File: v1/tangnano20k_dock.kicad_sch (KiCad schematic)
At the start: 54 parts, among them J1 Mini-DIN-6, J2 Conn_01x02, J3 DB15_Female_HighDensity_Mount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, J4 DB9_Male_MountingHoles, J5 Conn_02x10_Odd_Even, J6 Conn_02x10_Odd_Even, J7 RCA, J8 FCR684205T, J9 AudioJack3, U1 TXS0104E, U2 TangNano20K, U3 CS4354

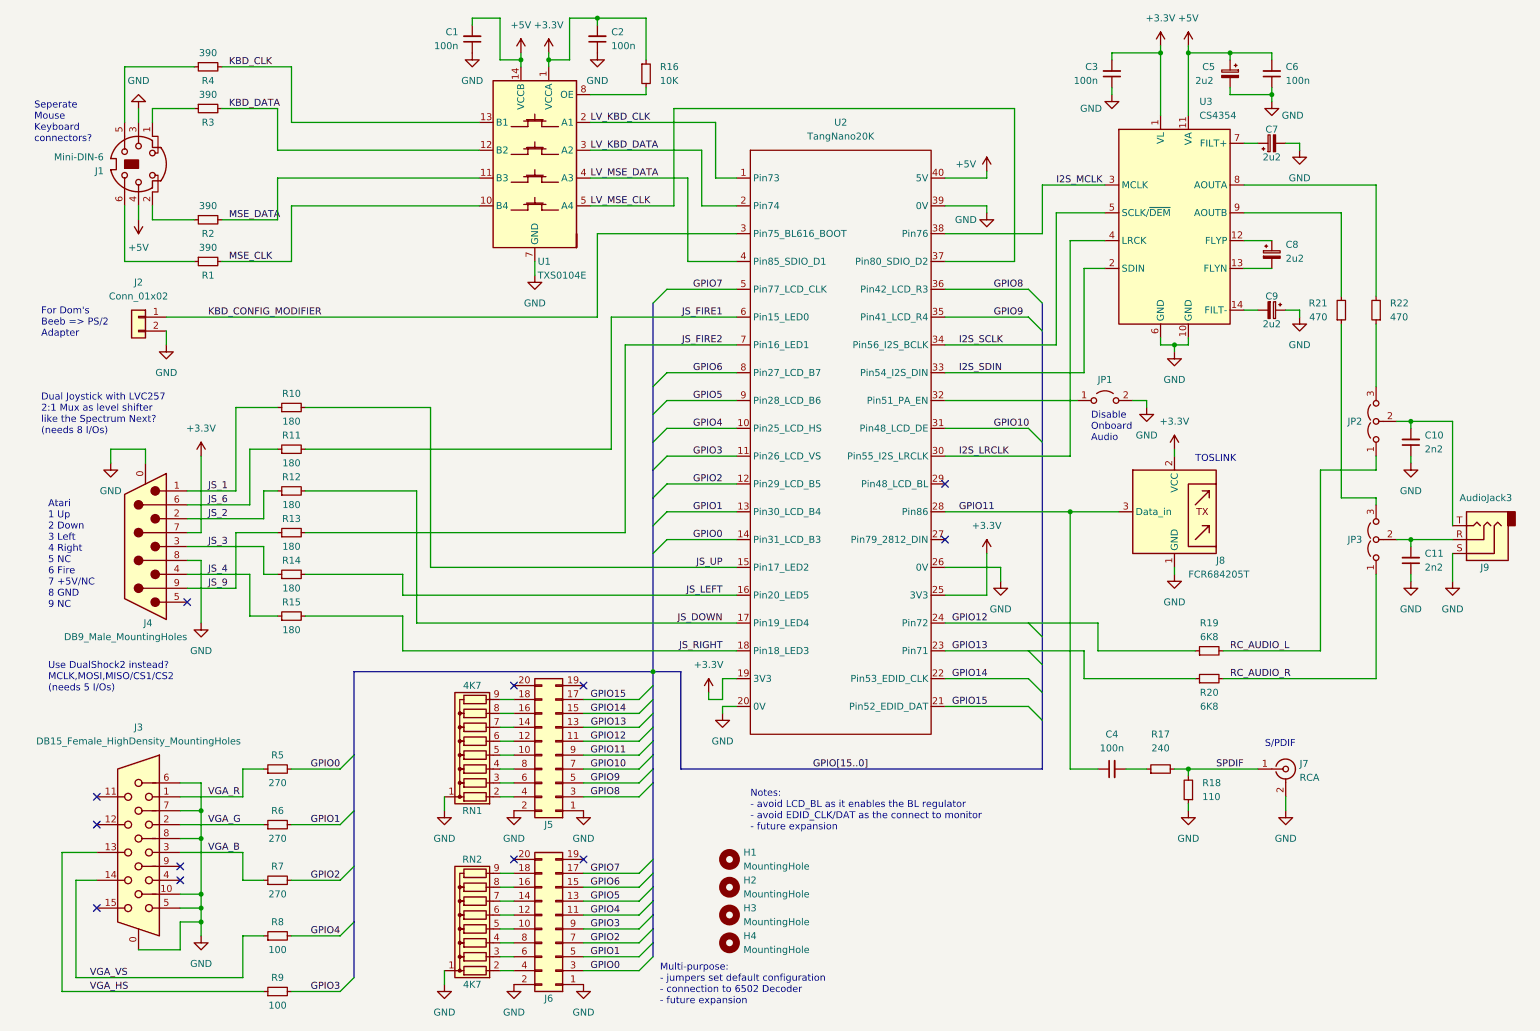
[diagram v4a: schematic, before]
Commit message: Start again, using 1206 SMT
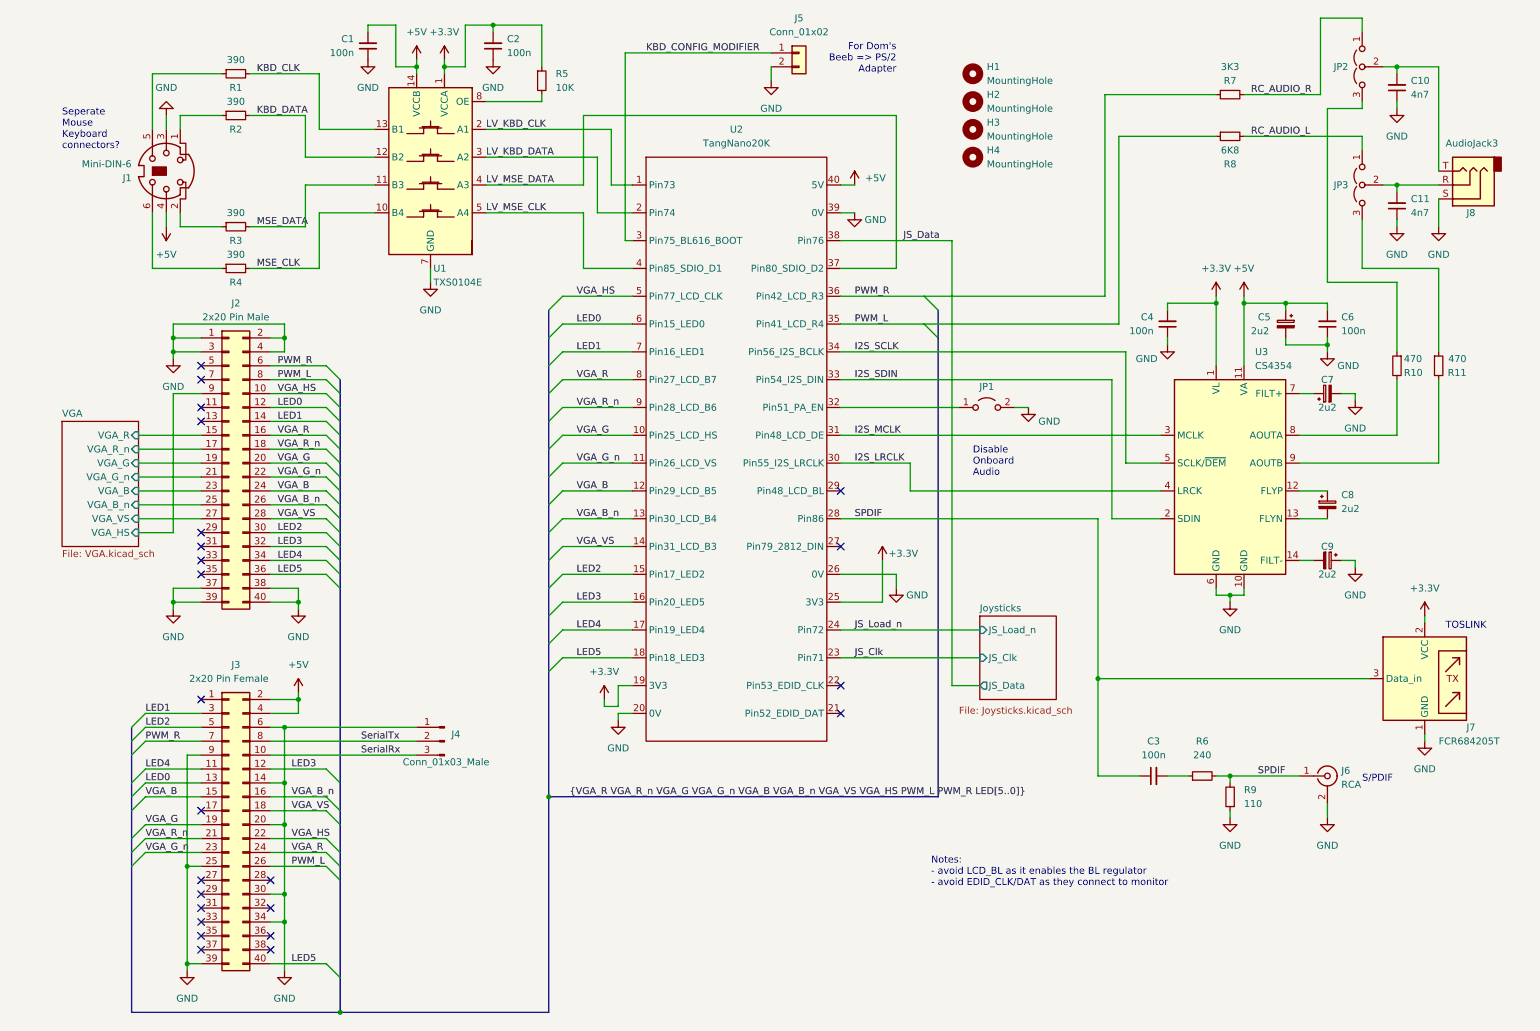
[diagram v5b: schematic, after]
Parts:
- removed J3: DB15_Female_HighDensity_MountingHoles, TangNano20k:DSUB-15-HD_Female_Horizontal_P2.29x1.98mm_EdgePinOffset8.35mm_Housed_MountingHolesOffset10.89mm, symbol Connector:DB15_Female_HighDensity_MountingHoles
- removed J4: DB9_Male_MountingHoles, Connector_Dsub:DSUB-9_Male_Horizontal_P2.77x2.84mm_EdgePinOffset7.70mm_Housed_MountingHolesOffset9.12mm, symbol Connector:DB9_Male_MountingHoles
- removed J5, J6: Conn_02x10_Odd_Even, Connector_PinHeader_2.54mm:PinHeader_2x10_P2.54mm_Vertical, symbol Connector_Generic:Conn_02x10_Odd_Even
- removed R10, R11, R12, R13, R14, R15: 180, Resistor_THT:R_Axial_DIN0207_L6.3mm_D2.5mm_P10.16mm_Horizontal, symbol Device:R_Small
- removed R5, R6, R7: 270, Resistor_THT:R_Axial_DIN0207_L6.3mm_D2.5mm_P10.16mm_Horizontal, symbol Device:R_Small
- removed R8, R9: 100, Resistor_THT:R_Axial_DIN0207_L6.3mm_D2.5mm_P10.16mm_Horizontal, symbol Device:R_Small
- removed RN1, RN2: 4K7, Resistor_THT:R_Array_SIP9, symbol Device:R_Network08
- added J2: 2x20 Pin Male, Connector_PinHeader_2.54mm:PinHeader_2x20_P2.54mm_Vertical, symbol Connector_Generic:Conn_02x20_Odd_Even
- added J3: 2x20 Pin Female, Connector_PinSocket_2.54mm:PinSocket_2x20_P2.54mm_Vertical, symbol Connector_Generic:Conn_02x20_Odd_Even
- added J4: Conn_01x03_Male, Connector_PinHeader_2.54mm:PinHeader_1x03_P2.54mm_Vertical, symbol Connector:Conn_01x03_Male
- C1, C2, C6: footprint Capacitor_THT:C_Disc_D4.3mm_W1.9mm_P5.00mm -> Capacitor_SMD:C_1206_3216Metric_Pad1.33x1.80mm_HandSolder
- C10, C11: value 2n2 -> 4n7; footprint Capacitor_THT:C_Disc_D5.0mm_W2.5mm_P2.50mm -> Capacitor_SMD:C_1206_3216Metric_Pad1.33x1.80mm_HandSolder
- C3: renamed from C4; footprint Capacitor_THT:C_Disc_D4.3mm_W1.9mm_P5.00mm -> Capacitor_SMD:C_1206_3216Metric_Pad1.33x1.80mm_HandSolder
- C4: renamed from C3; footprint Capacitor_THT:C_Disc_D4.3mm_W1.9mm_P5.00mm -> Capacitor_SMD:C_1206_3216Metric_Pad1.33x1.80mm_HandSolder
- C5, C7, C8, C9: footprint Capacitor_THT:CP_Radial_D5.0mm_P2.50mm -> Capacitor_SMD:C_1206_3216Metric_Pad1.33x1.80mm_HandSolder
- R1: renamed from R4; footprint Resistor_THT:R_Axial_DIN0207_L6.3mm_D2.5mm_P10.16mm_Horizontal -> Resistor_SMD:R_1206_3216Metric_Pad1.30x1.75mm_HandSolder
- R10: renamed from R22; footprint Resistor_THT:R_Axial_DIN0207_L6.3mm_D2.5mm_P10.16mm_Horizontal -> Resistor_SMD:R_1206_3216Metric_Pad1.30x1.75mm_HandSolder
- R11: renamed from R21; footprint Resistor_THT:R_Axial_DIN0207_L6.3mm_D2.5mm_P10.16mm_Horizontal -> Resistor_SMD:R_1206_3216Metric_Pad1.30x1.75mm_HandSolder
- R2: renamed from R3; footprint Resistor_THT:R_Axial_DIN0207_L6.3mm_D2.5mm_P10.16mm_Horizontal -> Resistor_SMD:R_1206_3216Metric_Pad1.30x1.75mm_HandSolder
- R3: renamed from R2; footprint Resistor_THT:R_Axial_DIN0207_L6.3mm_D2.5mm_P10.16mm_Horizontal -> Resistor_SMD:R_1206_3216Metric_Pad1.30x1.75mm_HandSolder
- R4: renamed from R1; footprint Resistor_THT:R_Axial_DIN0207_L6.3mm_D2.5mm_P10.16mm_Horizontal -> Resistor_SMD:R_1206_3216Metric_Pad1.30x1.75mm_HandSolder
- R5: renamed from R16; footprint Resistor_THT:R_Axial_DIN0207_L6.3mm_D2.5mm_P10.16mm_Horizontal -> Resistor_SMD:R_1206_3216Metric_Pad1.30x1.75mm_HandSolder
- R6: renamed from R17; footprint Resistor_THT:R_Axial_DIN0207_L6.3mm_D2.5mm_P10.16mm_Horizontal -> Resistor_SMD:R_1206_3216Metric_Pad1.30x1.75mm_HandSolder
- R7: renamed from R20; value 6K8 -> 3K3; footprint Resistor_THT:R_Axial_DIN0207_L6.3mm_D2.5mm_P10.16mm_Horizontal -> Resistor_SMD:R_1206_3216Metric_Pad1.30x1.75mm_HandSolder
- R8: renamed from R19; footprint Resistor_THT:R_Axial_DIN0207_L6.3mm_D2.5mm_P10.16mm_Horizontal -> Resistor_SMD:R_1206_3216Metric_Pad1.30x1.75mm_HandSolder
- R9: renamed from R18; footprint Resistor_THT:R_Axial_DIN0207_L6.3mm_D2.5mm_P10.16mm_Horizontal -> Resistor_SMD:R_1206_3216Metric_Pad1.30x1.75mm_HandSolder
- renumbered J2 to J5, J7 to J6, J8 to J7, J9 to J8, JP3 to JP2, JP2 to JP3
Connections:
- net GPIO0 is gone; now on net VGA_VS: U2.14 (Pin31_LCD_B3)
- net GPIO10 is gone; now on net I2S_MCLK: U2.31 (Pin48_LCD_DE)
- net GPIO11 is gone; now on net SPDIF: C3.1, J7.3 (Data_in), U2.28 (Pin86)
- net GPIO2 is gone; now on net VGA_B: U2.12 (Pin29_LCD_B5)
- net GPIO4 is gone; now on net VGA_G: U2.10 (Pin25_LCD_HS)
- net GPIO6 is gone; now on net VGA_R: U2.8 (Pin27_LCD_B7)
- net GPIO7 is gone; now on net VGA_HS: U2.5 (Pin77_LCD_CLK)
- net +5V: now also J3.2 (Pin_2), J3.4 (Pin_4)
- net GND: now also J2.1 (Pin_1), J2.2 (Pin_2), J2.3 (Pin_3), J2.37 (Pin_37), J2.38 (Pin_38), J2.39 (Pin_39), J2.4 (Pin_4), J2.40 (Pin_40), J3.14 (Pin_14), J3.20 (Pin_20), J3.25 (Pin_25), J3.30 (Pin_30), J3.34 (Pin_34), J3.39 (Pin_39), J3.6 (Pin_6), J3.9 (Pin_9), J4.1 (Pin_1)
- net I2S_MCLK: no longer U2.38 (Pin76)
- net LV_MSE_CLK: now also U2.4 (Pin85_SDIO_D1); no longer U2.37 (Pin80_SDIO_D2)
- net LV_MSE_DATA: now also U2.37 (Pin80_SDIO_D2); no longer U2.4 (Pin85_SDIO_D1)
- net VGA_B: now also J2.24 (Pin_24), J3.15 (Pin_15)
- net VGA_G: now also J2.20 (Pin_20), J3.19 (Pin_19)
- net VGA_HS: now also J2.10 (Pin_10), J3.22 (Pin_22)
- net VGA_R: now also J2.16 (Pin_16), J3.24 (Pin_24)
- net VGA_VS: now also J2.28 (Pin_28), J3.18 (Pin_18)
- net at C11.2, J8.R: now also JP3.2 (C); no longer JP2.2 (C)
- net at C10.2, J8.T: now also JP2.2 (C); no longer JP3.2 (C)
- net at JP2.3 (B): now also R10.1; no longer R11.1
- net at JP3.3 (B): now also R11.1; no longer R10.1
- net GPIO1 renamed VGA_B_n
- net VGA_B_n: now also J2.26 (Pin_26), J3.16 (Pin_16)
- net GPIO12 renamed JS_Load_n
- net JS_Load_n: no longer R8.1
- net GPIO13 renamed JS_Clk
- net JS_Clk: no longer R7.1
- net GPIO14: no longer names the net of U2.22 (Pin53_EDID_CLK)
- net GPIO15: no longer names the net of U2.21 (Pin52_EDID_DAT)
- net GPIO3 renamed VGA_G_n
- net VGA_G_n: now also J2.22 (Pin_22), J3.23 (Pin_23)
- net GPIO5 renamed VGA_R_n
- net VGA_R_n: now also J2.18 (Pin_18), J3.21 (Pin_21)
- net GPIO8 renamed PWM_R
- net PWM_R: now also R7.1, J2.6 (Pin_6), J3.7 (Pin_7)
- net GPIO9 renamed PWM_L
- net PWM_L: now also R8.1, J2.8 (Pin_8), J3.26 (Pin_26)
- net JS_DOWN renamed LED4
- net LED4: now also J2.34 (Pin_34), J3.11 (Pin_11)
- net JS_FIRE1 renamed LED0
- net LED0: now also J2.12 (Pin_12), J3.13 (Pin_13)
- net JS_FIRE2 renamed LED1
- net LED1: now also J2.14 (Pin_14), J3.3 (Pin_3)
- net JS_LEFT renamed LED3
- net LED3: now also J2.32 (Pin_32), J3.12 (Pin_12)
- net JS_RIGHT renamed LED5
- net LED5: now also J2.36 (Pin_36), J3.40 (Pin_40)
- net JS_UP renamed LED2
- net LED2: now also J2.30 (Pin_30), J3.5 (Pin_5)
- new net JS_Data: U2.38 (Pin76)
- new net SerialRx: J3.10 (Pin_10), J4.3 (Pin_3)
- new net SerialTx: J3.8 (Pin_8), J4.2 (Pin_2)
- new net VGA/VGA_B: J2.23 (Pin_23)
- new net VGA/VGA_B_n: J2.25 (Pin_25)
- new net VGA/VGA_G: J2.19 (Pin_19)
- new net VGA/VGA_G_n: J2.21 (Pin_21)
- new net VGA/VGA_HS: J2.9 (Pin_9)
- new net VGA/VGA_R: J2.15 (Pin_15)
- new net VGA/VGA_R_n: J2.17 (Pin_17)
- new net VGA/VGA_VS: J2.27 (Pin_27)
- no-connect marks 12 -> 24
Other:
- added sheet Joysticks (Joysticks.kicad_sch)
- added sheet VGA (VGA.kicad_sch)
- note added: "Notes: - avoid LCD_BL as it enables the BL regulator - avoid EDID_CLK/DAT as they connect to monitor"
- note removed: "Atari 1 Up 2 Down 3 Left 4 Right 5 NC 6 Fire 7 +5V/NC 8 GND 9 NC"
- note removed: "Dual Joystick with LVC257 2:1 Mux as level shifter like the Spectrum Next? (needs 8 I/Os)"
- note removed: "Multi-purpose: - jumpers set default configuration - connection to 6502 Decoder - future expansion"
- note removed: "Notes: - avoid LCD_BL as it enables the BL regulator - avoid EDID_CLK/DAT as the connect to monitor - future expansion"
- note removed: "Use DualShock2 instead? MCLK,MOSI,MISO/CS1/CS2 (needs 5 I/Os)"
- moved on the sheet: C1, C10, C11, C2, C3, C4, C5, C6, C7, C8, C9, H1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

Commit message: Work in progress
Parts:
- removed J2: 2x20 Pin Male, Connector_PinHeader_2.54mm:PinHeader_2x20_P2.54mm_Vertical, symbol Connector_Generic:Conn_02x20_Odd_Even
- added J3: Conn_01x20, Connector_PinHeader_2.54mm:PinHeader_1x20_P2.54mm_Vertical, symbol Connector_Generic:Conn_01x20
- R8: value 6K8 -> 3K3
- renumbered J3 to J2
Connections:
- net GND: now also JP1.1 (A), J3.1 (Pin_1), J3.19 (Pin_19), J3.2 (Pin_2), J3.20 (Pin_20); no longer JP1.2 (B)
- net LED0: now also J3.6 (Pin_6)
- net LED1: now also J2.12 (Pin_12), J3.7 (Pin_7); no longer J2.3 (Pin_3)
- net LED2: now also J2.11 (Pin_11), J3.15 (Pin_15); no longer J2.5 (Pin_5)
- net LED3: now also J2.7 (Pin_7), J3.16 (Pin_16); no longer J2.12 (Pin_12)
- net LED4: now also J2.5 (Pin_5), J3.17 (Pin_17); no longer J2.11 (Pin_11)
- net LED5: now also J2.3 (Pin_3), J3.18 (Pin_18); no longer J2.40 (Pin_40)
- net PWM_L: now also R8.2, J3.4 (Pin_4); no longer R8.1
- net PWM_R: now also J2.40 (Pin_40), R7.2, J3.3 (Pin_3); no longer J2.7 (Pin_7), R7.1
- net RC_AUDIO_L: now also R8.1; no longer R8.2
- net RC_AUDIO_R: now also R7.1; no longer R7.2
- net SPDIF: no longer J6.1 (In), R6.2, R9.2
- net VGA_B: now also J2.19 (Pin_19), J3.12 (Pin_12); no longer J2.15 (Pin_15)
- net VGA_B_n: now also J2.18 (Pin_18), J3.13 (Pin_13); no longer J2.16 (Pin_16)
- net VGA_G: now also J2.22 (Pin_22), J3.10 (Pin_10); no longer J2.19 (Pin_19)
- net VGA_G_n: now also J2.21 (Pin_21), J3.11 (Pin_11); no longer J2.23 (Pin_23)
- net VGA_HS: now also J2.15 (Pin_15), J3.5 (Pin_5); no longer J2.22 (Pin_22)
- net VGA_R: now also J3.8 (Pin_8)
- net VGA_R_n: now also J2.23 (Pin_23), J3.9 (Pin_9); no longer J2.21 (Pin_21)
- net VGA_VS: now also J2.16 (Pin_16), J3.14 (Pin_14); no longer J2.18 (Pin_18)
- net at U2.32 (Pin51_PA_EN): now also JP1.2 (B); no longer JP1.1 (A)
- new net: J6.1 (In), R6.2, R9.2
- no-connect marks 24 -> 16
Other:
- moved on the sheet: R7, R8

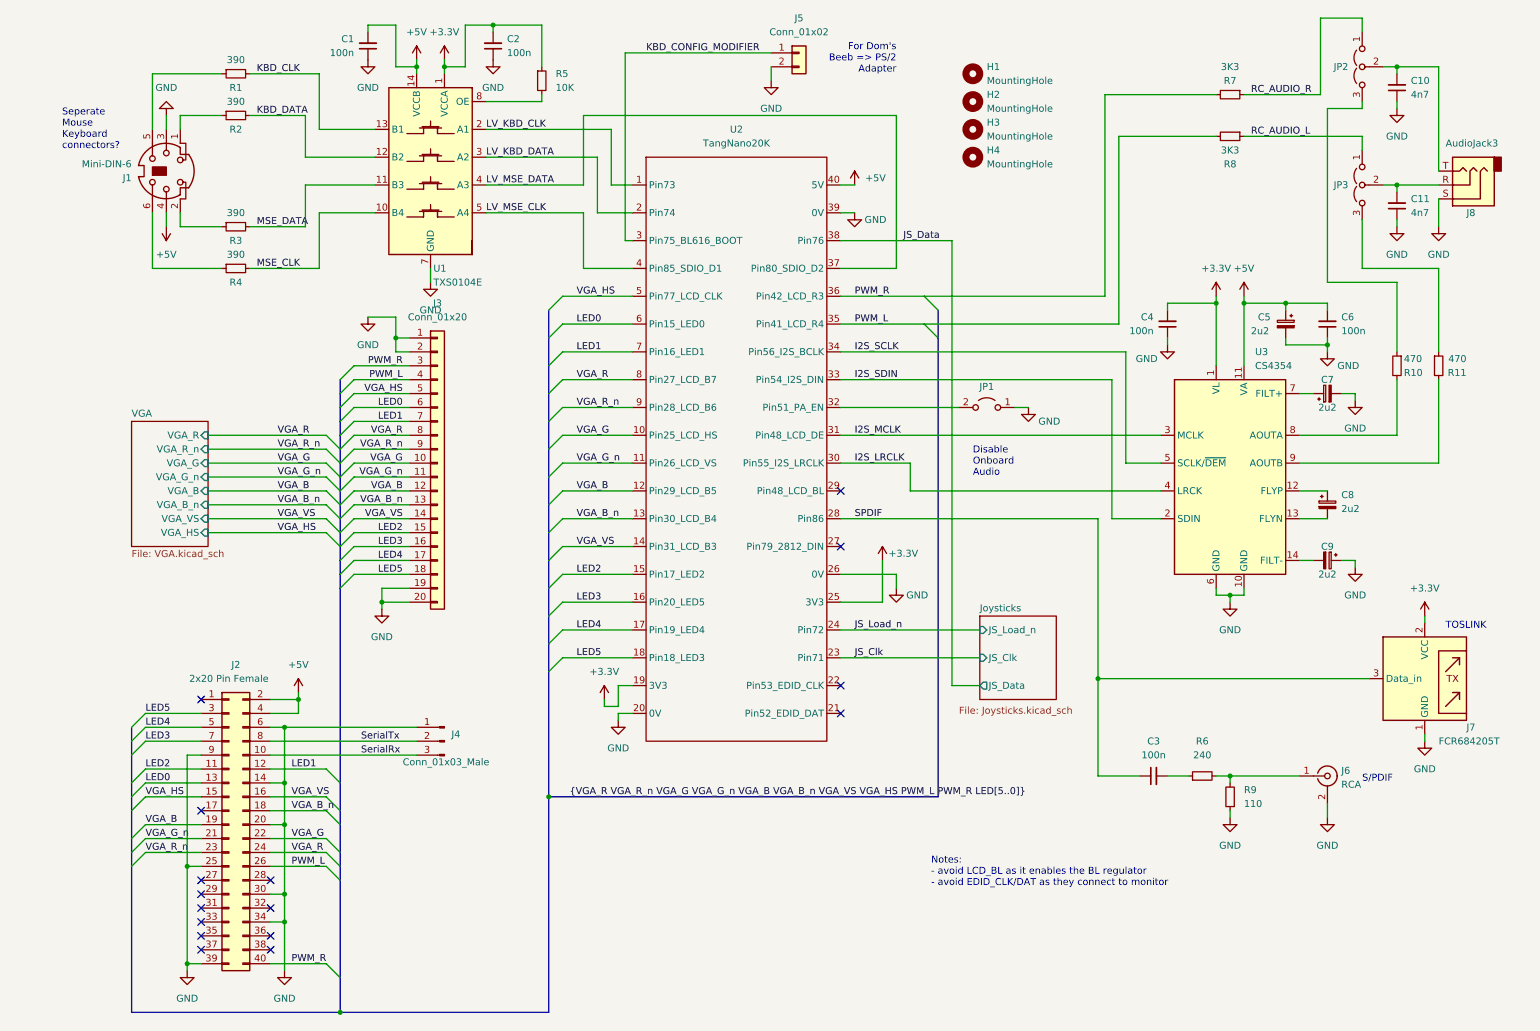
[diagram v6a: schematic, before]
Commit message: Updated VGA jumper block from 2x6 to 3x6
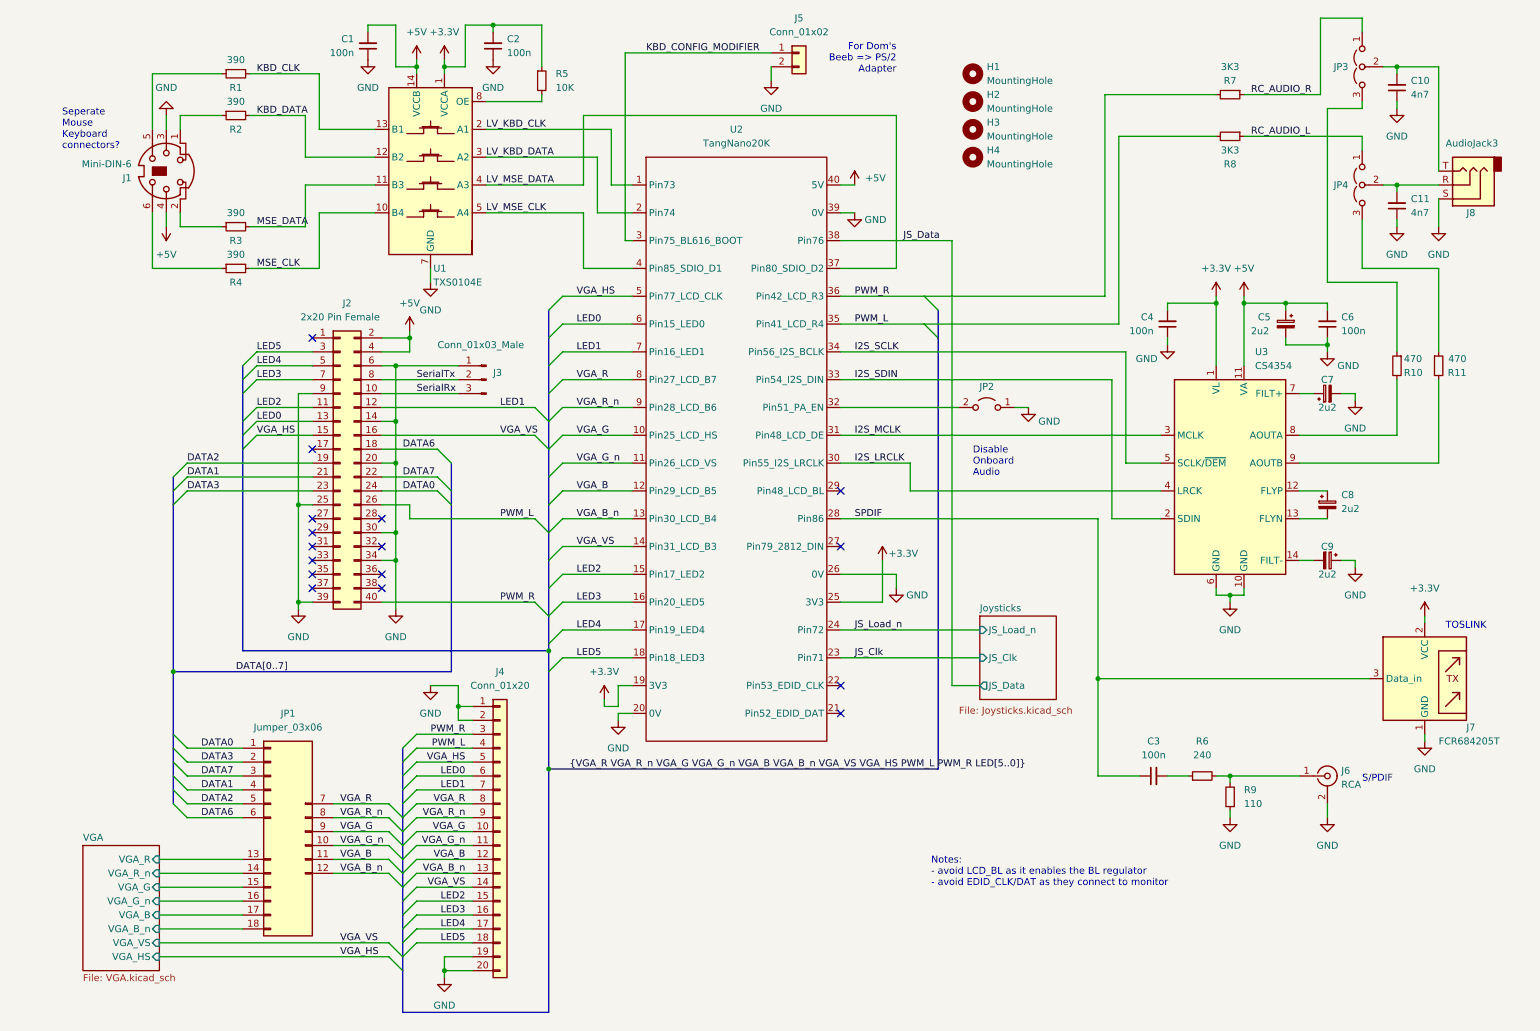
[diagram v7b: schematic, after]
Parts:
- added JP1: Jumper_03x06, TangNano20k:PinHeader_3x06_P2.54mm_Vertical, symbol TangNano20k:Jumper_03x06
- renumbered J4 to J3, J3 to J4, JP1 to JP2, JP2 to JP3, JP3 to JP4
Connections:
- net VGA_B: now also JP1.11 (Pin_11); no longer J2.19 (Pin_19)
- net VGA_B_n: now also JP1.12 (Pin_12); no longer J2.18 (Pin_18)
- net VGA_G: now also JP1.9 (Pin_9); no longer J2.22 (Pin_22)
- net VGA_G_n: now also JP1.10 (Pin_10); no longer J2.21 (Pin_21)
- net VGA_R: now also JP1.7 (Pin_7); no longer J2.24 (Pin_24)
- net VGA_R_n: now also JP1.8 (Pin_8); no longer J2.23 (Pin_23)
- new net DATA0: J2.24 (Pin_24), JP1.1 (Pin_1)
- new net DATA1: J2.21 (Pin_21), JP1.4 (Pin_4)
- new net DATA2: J2.19 (Pin_19), JP1.5 (Pin_5)
- new net DATA3: J2.23 (Pin_23), JP1.2 (Pin_2)
- new net DATA6: J2.18 (Pin_18), JP1.6 (Pin_6)
- new net DATA7: J2.22 (Pin_22), JP1.3 (Pin_3)
- new net VGA/VGA_B: JP1.17 (Pin_17)
- new net VGA/VGA_B_n: JP1.18 (Pin_18)
- new net VGA/VGA_G: JP1.15 (Pin_15)
- new net VGA/VGA_G_n: JP1.16 (Pin_16)
- new net VGA/VGA_R: JP1.13 (Pin_13)
- new net VGA/VGA_R_n: JP1.14 (Pin_14)
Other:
- moved on the sheet: J2, J3, J4
